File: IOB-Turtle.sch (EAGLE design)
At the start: 22 parts, among them J1 RJ12/6, Q1 P-FET, Q2 P-FET, Q3 P-FET, Q4 P-FET

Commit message: Version 2.0
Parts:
- removed FID3: FIDUCIAL, SPCoast:FIDUCIAL
- removed IOB: IO4-IOBBARE, SPCoast:IO4-IOBBARE
- removed LED1, LED3: G, SPCoast:LED0603-LED
- removed LED2: Y, SPCoast:LED0603-LED
- removed LED4: R, SPCoast:LED0603-LED
- removed Q1, Q2, Q3, Q4: P-FET, SPCoast:MOSFET-P
- removed R11, R12, R13, R14: 2k0, SPCoast:R0805-RES
- added R1, R2, R3: 10k, SPCoast:R0805-RES
- added U$1: CONNECTOR-IO4-IOBBARE, SPCoast:CONNECTOR-IO4-IOBBARE
- J1: device SPCoast:CONNECTOR-RJ25CORCOM -> SPCoast:CONNECTOR-IO4IPINS
- R5, R6, R7: value 1k0 -> 200R
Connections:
- net !KT renamed IO4-5
- removed net N$11: Q4.D, R14.2
- removed net N$2: LED4.A, R14.1
- removed net N$3: LED3.A, R13.1
- removed net N$30: Q3.D, R13.2
- removed net N$31: Q2.D, R12.2
- removed net N$32: Q1.D, R11.2
- removed net N$4: LED2.A, R12.1
- removed net N$5: LED1.A, R11.1
- removed net P1: IOB.P1, Q4.G, R7.2
- removed net P2: IOB.P2, Q3.G, R6.2
- removed net P3: IOB.P3, Q2.G, R5.2
- new net IO4-2: J1.2, R7.2
- new net IO4-3: J1.3, R5.2
- new net IO4-4: J1.4, R6.2
- net !NORM: now also R2.2, R5.1, U$1.P2; no longer J1.3, R6.1
- net !OCC: now also R3.2, R6.1, U$1.P3; no longer J1.4, R5.1
- net !REV: now also R1.2, U$1.P1; no longer J1.2
- net GND: now also U$1.GND; no longer IOB.GND, LED1.C, LED2.C, LED3.C, LED4.C
- net P4: now also U$1.P4; no longer IOB.P4, Q1.G
- net VCC: now also R1.1, R2.1, R3.1, U$1.5V; no longer IOB.5V, Q1.S, Q2.S, Q3.S, Q4.S
- net VCCIO: now also U$1.VIN; no longer IOB.VIN
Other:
- note added: "2.0"
- note added: "A"
- note removed: "1.0"
- note removed: "C"
- moved on the sheet: D1, R4, R5, R6, R7

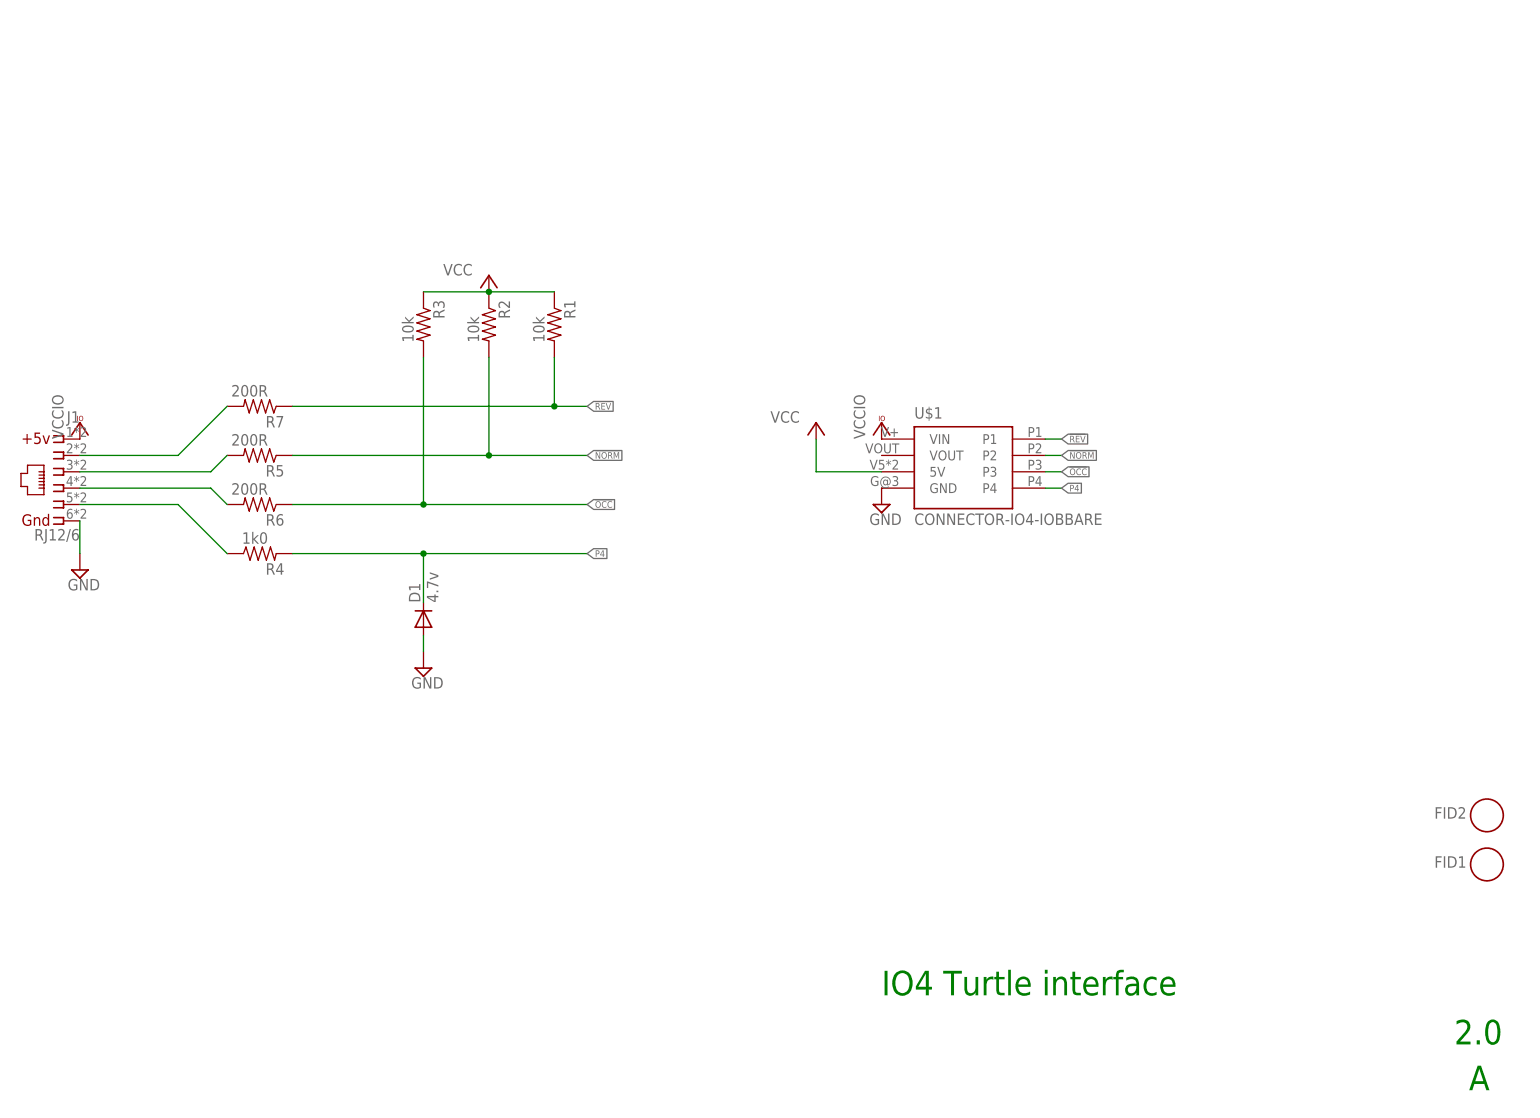
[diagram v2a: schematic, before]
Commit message: add lpf on inputs, normalized silkscreen layout across IOBs
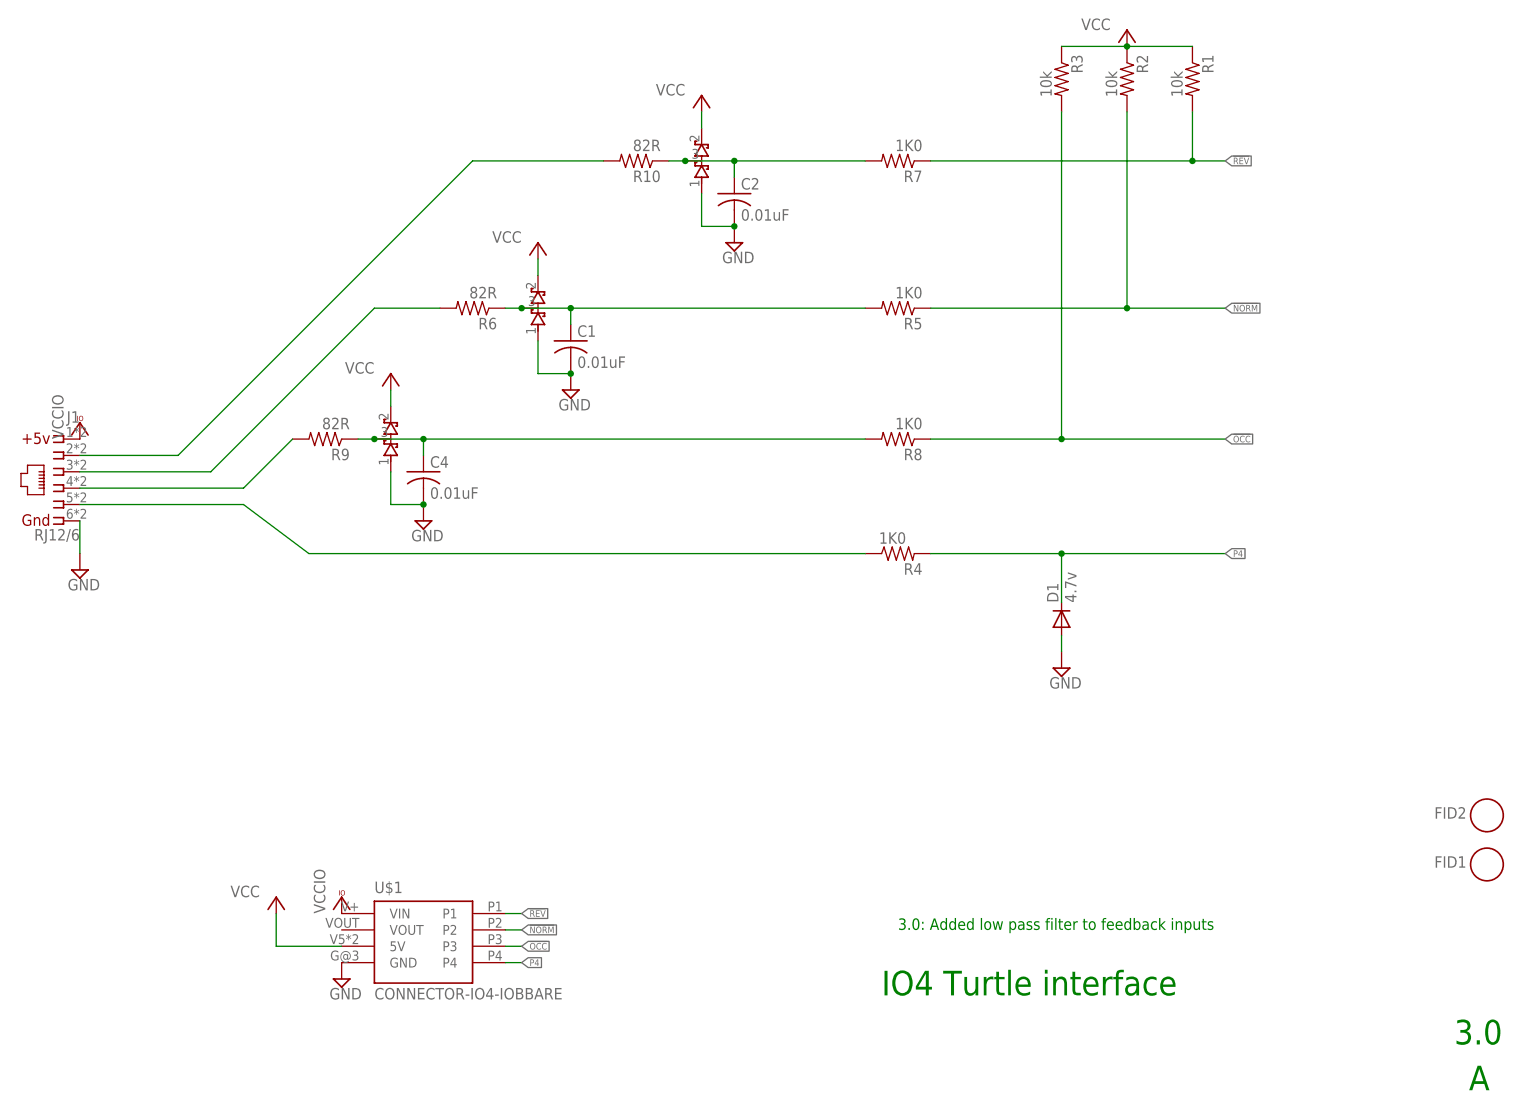
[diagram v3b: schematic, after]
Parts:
- added C1, C2, C4: 0.01uF, SPCoast:CAP0603
- added D2, D3, D4: BAT54S, SPCoast:DIODE-BAT54S23
- added R10, R9: 82R, SPCoast:R0805-RES
- added R8: 1K0, SPCoast:R0603-RES
- R4: value 1k0 -> 1K0; device SPCoast:R0805-RES -> SPCoast:R0603-RES
- R5, R7: value 200R -> 1K0; device SPCoast:R0805-RES -> SPCoast:R0603-RES
- R6: value 200R -> 82R
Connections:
- removed net IO4-4: J1.4, R6.2
- new net N$1: J1.4, R9.2
- new net N$14: C4.1, D4.COM, R8.2, R9.1
- new net N$2: C1.1, D2.COM, R5.2, R6.1
- new net N$3: C2.1, D3.COM, R10.1, R7.2
- net !OCC: now also R8.1; no longer R6.1
- net GND: now also C1.2, C2.2, C4.2, D2.A1, D3.A1, D4.A1
- net IO4-2: now also R10.2; no longer R7.2
- net IO4-3: now also R6.2; no longer R5.2
- net VCC: now also D2.C2, D3.C2, D4.C2
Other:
- note added: "3.0"
- note added: "3.0: Added low pass filter to feedback inputs"
- note removed: "2.0"
- moved on the sheet: D1, R1, R2, R3, R4, R5, R6, R7, U$1
